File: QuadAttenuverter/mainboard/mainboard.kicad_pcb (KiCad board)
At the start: 2 copper layers, 35.6 x 108 mm, 65 parts, among them U1 LM324, U2 LM324, U3 LM324, U4 LM324, U5 LM324

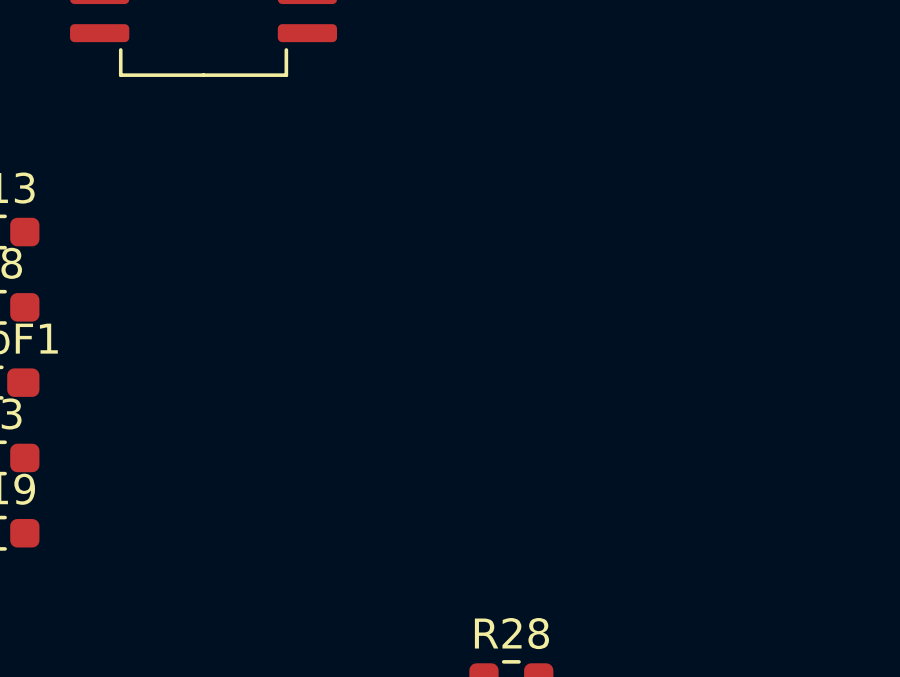
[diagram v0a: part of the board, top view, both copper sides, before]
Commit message: Add resistors to make pots more center sensitive
Idea from here:
https://kassu2000.blogspot.com/2018/04/precision-attenuverter-mixer.html
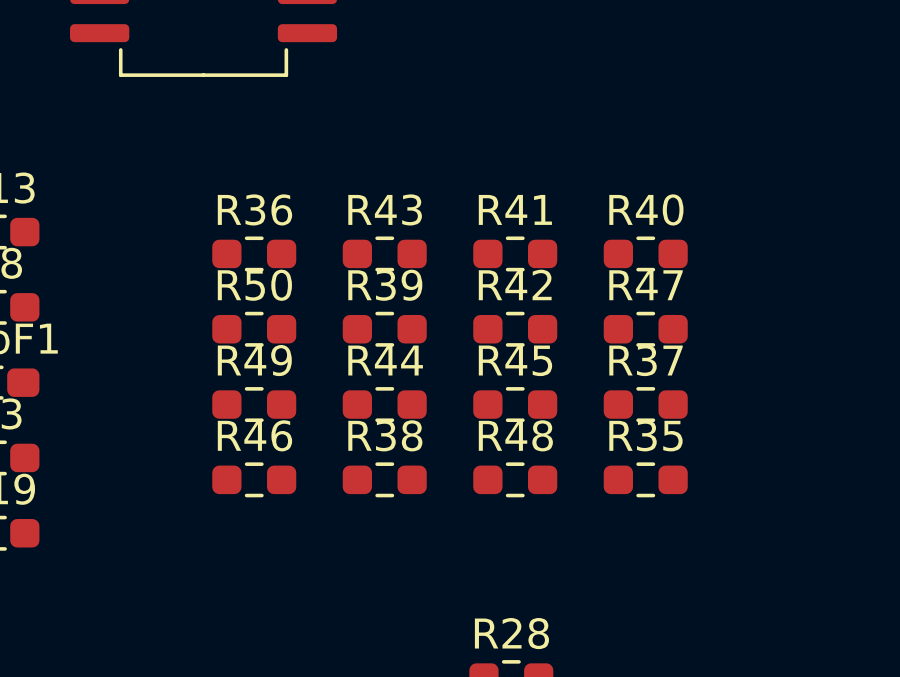
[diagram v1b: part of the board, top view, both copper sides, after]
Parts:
- added R35: 47k, Resistor_SMD:R_0603_1608Metric_Pad0.98x0.95mm_HandSolder, F.Cu at (208.8, 121.5)
- added R36: 47k, Resistor_SMD:R_0603_1608Metric_Pad0.98x0.95mm_HandSolder, F.Cu at (195.8, 114.0)
- added R37: 47k, Resistor_SMD:R_0603_1608Metric_Pad0.98x0.95mm_HandSolder, F.Cu at (208.8, 119.0)
- added R38: 47k, Resistor_SMD:R_0603_1608Metric_Pad0.98x0.95mm_HandSolder, F.Cu at (200.1, 121.5)
- added R39: 47k, Resistor_SMD:R_0603_1608Metric_Pad0.98x0.95mm_HandSolder, F.Cu at (200.1, 116.5)
- added R40: 47k, Resistor_SMD:R_0603_1608Metric_Pad0.98x0.95mm_HandSolder, F.Cu at (208.8, 114.0)
- added R41: 47k, Resistor_SMD:R_0603_1608Metric_Pad0.98x0.95mm_HandSolder, F.Cu at (204.4, 114.0)
- added R42: 47k, Resistor_SMD:R_0603_1608Metric_Pad0.98x0.95mm_HandSolder, F.Cu at (204.4, 116.5)
- added R43: 47k, Resistor_SMD:R_0603_1608Metric_Pad0.98x0.95mm_HandSolder, F.Cu at (200.1, 114.0)
- added R44: 47k, Resistor_SMD:R_0603_1608Metric_Pad0.98x0.95mm_HandSolder, F.Cu at (200.1, 119.0)
- added R45: 47k, Resistor_SMD:R_0603_1608Metric_Pad0.98x0.95mm_HandSolder, F.Cu at (204.4, 119.0)
- added R46: 47k, Resistor_SMD:R_0603_1608Metric_Pad0.98x0.95mm_HandSolder, F.Cu at (195.8, 121.5)
- added R47: 47k, Resistor_SMD:R_0603_1608Metric_Pad0.98x0.95mm_HandSolder, F.Cu at (208.8, 116.5)
- added R48: 47k, Resistor_SMD:R_0603_1608Metric_Pad0.98x0.95mm_HandSolder, F.Cu at (204.4, 121.5)
- added R49: 47k, Resistor_SMD:R_0603_1608Metric_Pad0.98x0.95mm_HandSolder, F.Cu at (195.8, 119.0)
- added R50: 47k, Resistor_SMD:R_0603_1608Metric_Pad0.98x0.95mm_HandSolder, F.Cu at (195.8, 116.5)

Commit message: Final preparations for board splitup
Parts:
- added J1: Conn_01x09, Connector_PinHeader_2.54mm:PinHeader_1x09_P2.54mm_Vertical, F.Cu at (101.0, 115.8)
- added J2: Conn_02x10_Counter_Clockwise, Connector_PinHeader_2.54mm:PinHeader_2x10_P2.54mm_Vertical, F.Cu at (89.7, 45.6)
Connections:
- net Net-(IN1-PadT) renamed /IN1
- net Net-(IN2-PadT) renamed /IN3
- net Net-(IN3-PadT) renamed /IN2
- net Net-(IN4-PadT) renamed /IN4
- net Net-(OUT1-PadT) renamed /OUT1
- net Net-(OUT2-PadT) renamed /OUT3
- net Net-(OUT3-PadT) renamed /OUT2
- net Net-(OUT4-PadT) renamed /OUT4
- net Net-(R13-Pad1) renamed /GAIN3IN
- net Net-(R14-Pad1) renamed /GAIN2IN
- net Net-(R15-Pad1) renamed /GAIN4IN
- net Net-(R2-Pad1) renamed /GAIN1IN
- net Net-(R35-Pad2) renamed /GAIN3OUT
- net Net-(R36-Pad2) renamed /GAIN1OUT
- net Net-(R37-Pad2) renamed /GAIN2OUT
- net Net-(R38-Pad2) renamed /GAIN4OUT
- net Net-(R43-Pad2) renamed /OFFSET3
- net Net-(R45-Pad2) renamed /OFFSET1
- net Net-(R47-Pad2) renamed /OFFSET2
- net Net-(R49-Pad2) renamed /OFFSET4
- D1 pad 1: Net-(D1-Pad1) -> GND
- D1 pad 2: Net-(D1-Pad2) -> /LED1
- D2 pad 1: Net-(D2-Pad1) -> GND
- D2 pad 2: Net-(D2-Pad2) -> /LED2
- D3 pad 1: Net-(D3-Pad1) -> GND
- D3 pad 2: Net-(D3-Pad2) -> /LED3
- D4 pad 1: Net-(D4-Pad1) -> GND
- D4 pad 2: Net-(D4-Pad2) -> /LED4
- R31 pad 1: Net-(D1-Pad1) -> Net-(R31-Pad1)
- R31 pad 2: GND -> /LED1
- R32 pad 1: Net-(D2-Pad1) -> Net-(R32-Pad1)
- R32 pad 2: GND -> /LED2
- R33 pad 1: Net-(D3-Pad1) -> Net-(R33-Pad1)
- R33 pad 2: GND -> /LED3
- R34 pad 1: Net-(D4-Pad1) -> Net-(R34-Pad1)
- R34 pad 2: GND -> /LED4
- U5 pad 1: Net-(D1-Pad2) -> Net-(R31-Pad1)
- U5 pad 14: Net-(D4-Pad2) -> Net-(R34-Pad1)
- U5 pad 7: Net-(D2-Pad2) -> Net-(R32-Pad1)
- U5 pad 8: Net-(D3-Pad2) -> Net-(R33-Pad1)

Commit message: Fixed duplicate net names for LEDn
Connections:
- 22pF1 pad 2: /LED1 -> /LEDSIG1
- 22pF2 pad 2: /LED3 -> /LEDSIG3
- 22pF3 pad 2: /LED2 -> /LEDSIG2
- 22pF4 pad 2: /LED4 -> /LEDSIG4
- R28 pad 1: /LED3 -> /LEDSIG3
- R29 pad 1: /LED2 -> /LEDSIG2
- R30 pad 1: /LED4 -> /LEDSIG4
- R7 pad 1: /LED1 -> /LEDSIG1
- U1 pad 8: /LED1 -> /LEDSIG1
- U2 pad 8: /LED3 -> /LEDSIG3
- U3 pad 8: /LED2 -> /LEDSIG2
- U4 pad 8: /LED4 -> /LEDSIG4
- U5 pad 10: /LED3 -> /LEDSIG3
- U5 pad 12: /LED4 -> /LEDSIG4
- U5 pad 3: /LED1 -> /LEDSIG1
- U5 pad 5: /LED2 -> /LEDSIG2
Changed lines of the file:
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@@
   (net 57 "Net-(R33-Pad1)")
   (net 58 "Net-(R34-Pad1)")
+  (net 59 "/LEDSIG1")
+  (net 60 "/LEDSIG3")
+  (net 61 "/LEDSIG2")
+  (net 62 "/LEDSIG4")
   (footprint "Potentiometer_THT:Potentiometer_Alps_RK09K_Single_Vertical" (layer "F.Cu")
     (at 116.8 57.71 180)
@@
       (net 24 "Net-(R3-Pad2)") (pintype "output"))
     (pad "8" smd roundrect (at 3.4625 3.81) (size 1.975 0.6) (layers "F.Cu" "F.Paste" "F.Mask") (roundrect_rratio 0.25)
-      (net 2 "/LED1") (pintype "output"))
+      (net 59 "/LEDSIG1") (pintype "output"))
     (pad "9" smd roundrect (at 3.4625 2.54) (size 1.975 0.6) (layers "F.Cu" "F.Paste" "F.Mask") (roundrect_rratio 0.25)
       (net 1 "Net-(22pF1-Pad1)") (pinfunction "-") (pintype "input"))
@@
       (net 37 "Net-(R16-Pad2)") (pintype "output"))
     (pad "8" smd roundrect (at 3.4625 3.81) (size 1.975 0.6) (layers "F.Cu" "F.Paste" "F.Mask") (roundrect_rratio 0.25)
-      (net 51 "/LED3") (pintype "output"))
+      (net 60 "/LEDSIG3") (pintype "output"))
     (pad "9" smd roundrect (at 3.4625 2.54) (size 1.975 0.6) (layers "F.Cu" "F.Paste" "F.Mask") (roundrect_rratio 0.25)
       (net 3 "Net-(22pF2-Pad1)") (pinfunction "-") (pintype "input"))
@@
       (net 3 "Net-(22pF2-Pad1)") (pintype "passive"))
     (pad "2" smd roundrect (at 0.8625 0) (size 1.075 0.95) (layers "F.Cu" "F.Paste" "F.Mask") (roundrect_rratio 0.25)
-      (net 51 "/LED3") (pintype "passive"))
+      (net 60 "/LEDSIG3") (pintype "passive"))
     (model "${KICAD6_3DMODEL_DIR}/Capacitor_SMD.3dshapes/C_0603_1608Metric.wrl"
       (offset (xyz 0 0 0))
@@
       (net 4 "Net-(22pF3-Pad1)") (pintype "passive"))
     (pad "2" smd roundrect (at 0.8625 0) (size 1.075 0.95) (layers "F.Cu" "F.Paste" "F.Mask") (roundrect_rratio 0.25)
-      (net 52 "/LED2") (pintype "passive"))
+      (net 61 "/LEDSIG2") (pintype "passive"))
     (model "${KICAD6_3DMODEL_DIR}/Capacitor_SMD.3dshapes/C_0603_1608Metric.wrl"
       (offset (xyz 0 0 0))
@@
       (net 7 "GND") (pinfunction "-") (pintype "input"))
     (pad "3" smd roundrect (at -3.4625 -1.27) (size 1.975 0.6) (layers "F.Cu" "F.Paste" "F.Mask") (roundrect_rratio 0.25)
-      (net 2 "/LED1") (pinfunction "+") (pintype "input"))
+      (net 59 "/LEDSIG1") (pinfunction "+") (pintype "input"))
     (pad "4" smd roundrect (at -3.4625 0) (size 1.975 0.6) (layers "F.Cu" "F.Paste" "F.Mask") (roundrect_rratio 0.25)
       (net 26 "+12V") (pinfunction "V+") (pintype "power_in"))
     (pad "5" smd roundrect (at -3.4625 1.27) (size 1.975 0.6) (layers "F.Cu" "F.Paste" "F.Mask") (roundrect_rratio 0.25)
-      (net 52 "/LED2") (pinfunction "+") (pintype "input"))
+      (net 61 "/LEDSIG2") (pinfunction "+") (pintype "input"))
     (pad "6" smd roundrect (at -3.4625 2.54) (size 1.975 0.6) (layers "F.Cu" "F.Paste" "F.Mask") (roundrect_rratio 0.25)
       (net 7 "GND") (pinfunction "-") (pintype "input"))
@@
       (net 7 "GND") (pinfunction "-") (pintype "input"))
     (pad "10" smd roundrect (at 3.4625 1.27) (size 1.975 0.6) (layers "F.Cu" "F.Paste" "F.Mask") (roundrect_rratio 0.25)
-      (net 51 "/LED3") (pinfunction "+") (pintype "input"))
+      (net 60 "/LEDSIG3") (pinfunction "+") (pintype "input"))
     (pad "11" smd roundrect (at 3.4625 0) (size 1.975 0.6) (layers "F.Cu" "F.Paste" "F.Mask") (roundrect_rratio 0.25)
       (net 27 "-12V") (pinfunction "V-") (pintype "power_in"))
     (pad "12" smd roundrect (at 3.4625 -1.27) (size 1.975 0.6) (layers "F.Cu" "F.Paste" "F.Mask") (roundrect_rratio 0.25)
-      (net 53 "/LED4") (pinfunction "+") (pintype "input"))
+      (net 62 "/LEDSIG4") (pinfunction "+") (pintype "input"))
     (pad "13" smd roundrect (at 3.4625 -2.54) (size 1.975 0.6) (layers "F.Cu" "F.Paste" "F.Mask") (roundrect_rratio 0.25)
       (net 7 "GND") (pinfunction "-") (pintype "input"))
@@
     (fp_line (start 0.8 0.4125) (end -0.8 0.4125) (layer "F.Fab") (width 0.1))
     (pad "1" smd roundrect (at -0.9125 0) (size 0.975 0.95) (layers "F.Cu" "F.Paste" "F.Mask") (roundrect_rratio 0.25)
-      (net 51 "/LED3") (pintype "passive"))
+      (net 60 "/LEDSIG3") (pintype "passive"))
     (pad "2" smd roundrect (at 0.9125 0) (size 0.975 0.95) (layers "F.Cu" "F.Paste" "F.Mask") (roundrect_rratio 0.25)
       (net 17 "/OUT3") (pintype "passive"))
@@
       (net 5 "Net-(22pF4-Pad1)") (pintype "passive"))
     (pad "2" smd roundrect (at 0.8625 0) (size 1.075 0.95) (layers "F.Cu" "F.Paste" "F.Mask") (roundrect_rratio 0.25)
-      (net 53 "/LED4") (pintype "passive"))
+      (net 62 "/LEDSIG4") (pintype "passive"))
     (model "${KICAD6_3DMODEL_DIR}/Capacitor_SMD.3dshapes/C_0603_1608Metric.wrl"
       (offset (xyz 0 0 0))
@@
       (net 39 "Net-(R18-Pad2)") (pintype "output"))
     (pad "8" smd roundrect (at 3.4625 3.81) (size 1.975 0.6) (layers "F.Cu" "F.Paste" "F.Mask") (roundrect_rratio 0.25)
-      (net 53 "/LED4") (pintype "output"))
+      (net 62 "/LEDSIG4") (pintype "output"))
     (pad "9" smd roundrect (at 3.4625 2.54) (size 1.975 0.6) (layers "F.Cu" "F.Paste" "F.Mask") (roundrect_rratio 0.25)
       (net 5 "Net-(22pF4-Pad1)") (pinfunction "-") (pintype "input"))
@@
     (fp_line (start -0.8 0.4125) (end -0.8 -0.4125) (layer "F.Fab") (width 0.1))
     (pad "1" smd roundrect (at -0.9125 0) (size 0.975 0.95) (layers "F.Cu" "F.Paste" "F.Mask") (roundrect_rratio 0.25)
-      (net 52 "/LED2") (pintype "passive"))
+      (net 61 "/LEDSIG2") (pintype "passive"))
     (pad "2" smd roundrect (at 0.9125 0) (size 0.975 0.95) (layers "F.Cu" "F.Paste" "F.Mask") (roundrect_rratio 0.25)
       (net 15 "/OUT2") (pintype "passive"))
@@
       (net 38 "Net-(R17-Pad2)") (pintype "output"))
     (pad "8" smd roundrect (at 3.4625 3.81) (size 1.975 0.6) (layers "F.Cu" "F.Paste" "F.Mask") (roundrect_rratio 0.25)
-      (net 52 "/LED2") (pintype "output"))
+      (net 61 "/LEDSIG2") (pintype "output"))
     (pad "9" smd roundrect (at 3.4625 2.54) (size 1.975 0.6) (layers "F.Cu" "F.Paste" "F.Mask") (roundrect_rratio 0.25)
       (net 4 "Net-(22pF3-Pad1)") (pinfunction "-") (pintype "input"))
@@
     (fp_line (start -0.8 0.4125) (end -0.8 -0.4125) (layer "F.Fab") (width 0.1))
     (pad "1" smd roundrect (at -0.9125 0) (size 0.975 0.95) (layers "F.Cu" "F.Paste" "F.Mask") (roundrect_rratio 0.25)
-      (net 2 "/LED1") (pintype "passive"))
+      (net 59 "/LEDSIG1") (pintype "passive"))
     (pad "2" smd roundrect (at 0.9125 0) (size 0.975 0.95) (layers "F.Cu" "F.Paste" "F.Mask") (roundrect_rratio 0.25)
       (net 13 "/OUT1") (pintype "passive"))
@@
       (net 1 "Net-(22pF1-Pad1)") (pintype "passive"))
     (pad "2" smd roundrect (at 0.8625 0) (size 1.075 0.95) (layers "F.Cu" "F.Paste" "F.Mask") (roundrect_rratio 0.25)
-      (net 2 "/LED1") (pintype "passive"))
+      (net 59 "/LEDSIG1") (pintype "passive"))
     (model "${KICAD6_3DMODEL_DIR}/Capacitor_SMD.3dshapes/C_0603_1608Metric.wrl"
       (offset (xyz 0 0 0))
@@
     (fp_line (start 0.8 0.4125) (end -0.8 0.4125) (layer "F.Fab") (width 0.1))
     (pad "1" smd roundrect (at -0.9125 0) (size 0.975 0.95) (layers "F.Cu" "F.Paste" "F.Mask") (roundrect_rratio 0.25)
-      (net 53 "/LED4") (pintype "passive"))
+      (net 62 "/LEDSIG4") (pintype "passive"))
     (pad "2" smd roundrect (at 0.9125 0) (size 0.975 0.95) (layers "F.Cu" "F.Paste" "F.Mask") (roundrect_rratio 0.25)
       (net 19 "/OUT4") (pintype "passive"))

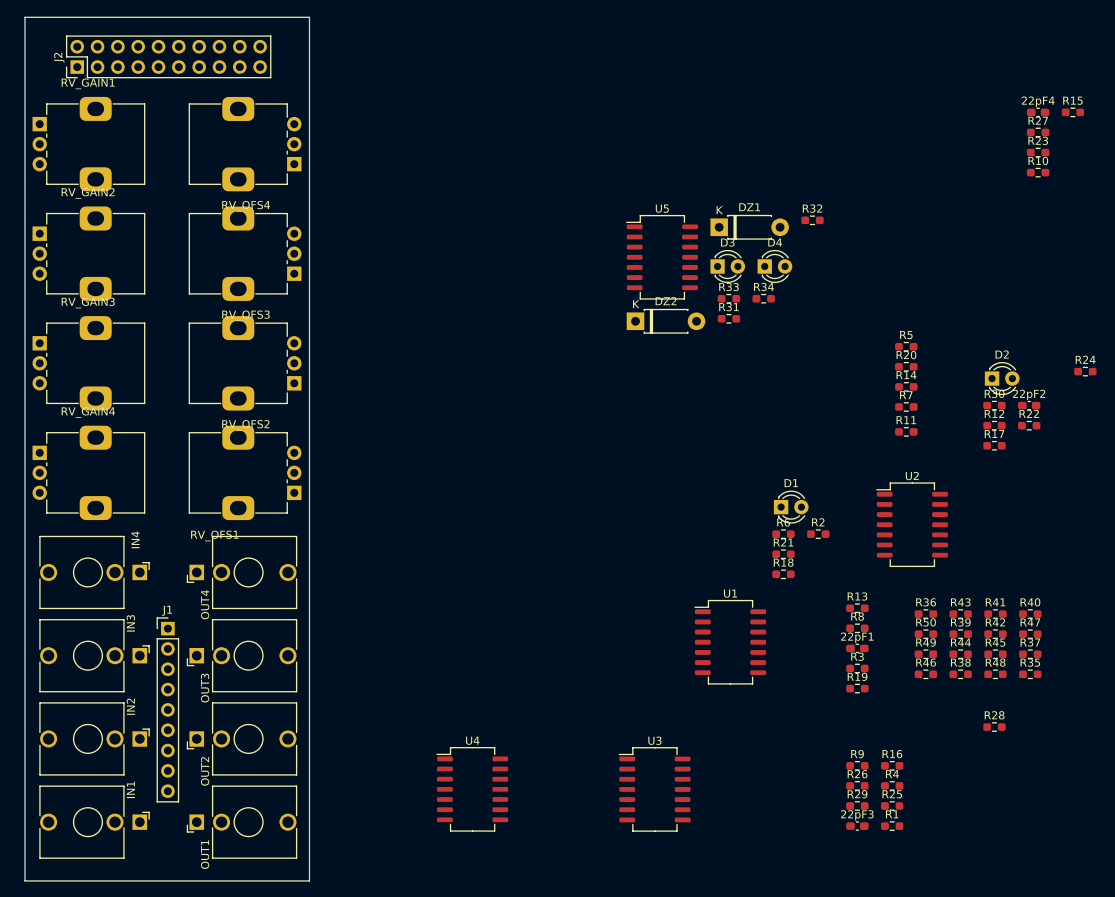
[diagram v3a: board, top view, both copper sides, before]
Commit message: Initial routing of ioboard
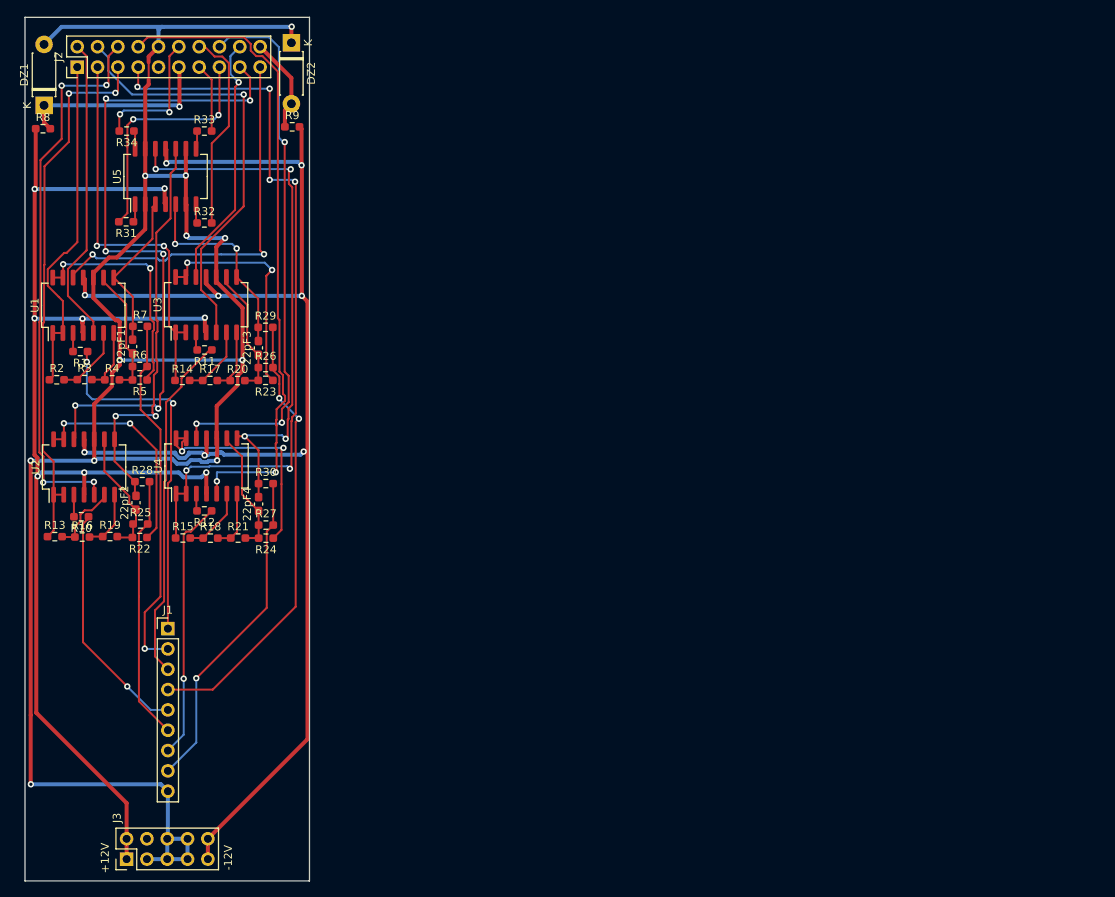
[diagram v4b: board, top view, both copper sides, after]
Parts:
- removed D1, D2, D3, D4: LED_Dual_Bidirectional, LED_THT:LED_D3.0mm
- removed IN1, IN2, IN3, IN4, OUT1, OUT2, OUT3, OUT4: AudioJack2_SwitchT, Connector_Audio:Jack_3.5mm_QingPu_WQP-PJ398SM_Vertical_CircularHoles
- removed R35, R36, R37, R38, R39, R40, R41, R42, R43, R44, R45, R46, R47, R48, R49, R50: 47k, Resistor_SMD:R_0603_1608Metric_Pad0.98x0.95mm_HandSolder
- removed RV_GAIN1, RV_GAIN2, RV_GAIN3, RV_GAIN4, RV_OFS1, RV_OFS2, RV_OFS3, RV_OFS4: 100k, Potentiometer_THT:Potentiometer_Alps_RK09K_Single_Vertical
- added J3: Conn_02x05_Odd_Even, Connector_PinHeader_2.54mm:PinHeader_2x05_P2.54mm_Vertical, F.Cu at (95.8, 144.6)
- moved R10 127.1 mm to (90.2, 101.8), turned to 180 degrees
- moved R15 123.3 mm to (102.9, 104.4)
- moved R8 119.4 mm to (85.4, 53.3)
- moved R1 117.6 mm to (90.0, 81.1), turned to 180 degrees
- moved 22pF2 112.3 mm to (97.0, 100.0), turned to 90 degrees
- moved R22 112.1 mm to (97.5, 104.4), turned to 180 degrees
- moved R28 110.9 mm to (97.8, 97.4)
- moved R4 109.9 mm to (94.0, 84.7)
- moved 22pF4 109.0 mm to (112.3, 100.2), turned to 90 degrees
- moved R27 108.3 mm to (113.3, 102.8)
- moved R9 106.6 mm to (116.5, 53.0)
- moved R16 105.2 mm to (90.3, 104.3)
- moved R24 104.5 mm to (113.3, 104.5), turned to 180 degrees
- moved U2 103.8 mm to (90.5, 95.6), turned to 90 degrees
- moved R3 103.1 mm to (90.6, 84.6)
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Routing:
- net GND: track 0.00 -> 263.2 mm, vias 0 -> 11
- net -12V: track 0.00 -> 181.1 mm, vias 0 -> 8
- net +12V: track 0.00 -> 167.4 mm, vias 0 -> 8
- net /GAIN4IN: track 0.00 -> 93.1 mm, vias 0 -> 6
- net /OFFSET3: track 0.00 -> 83.7 mm, vias 0 -> 6
- net /GAIN4OUT: track 0.00 -> 81.3 mm, vias 0 -> 2
- net /GAIN3OUT: track 0.00 -> 70.0 mm, vias 0 -> 4
- net /OFFSET4: track 0.00 -> 68.9 mm, vias 0 -> 3
- net /LEDSIG4: track 0.00 -> 68.5 mm, vias 0 -> 4
- net /GAIN3IN: track 0.00 -> 68.1 mm, vias 0 -> 2
- net /OUT2: track 0.00 -> 56.7 mm, vias 0 -> 2
- net /GAIN2OUT: track 0.00 -> 54.4 mm, vias 0 -> 1
- net /LEDSIG3: track 0.00 -> 51.3 mm, vias 0 -> 2
- net /OFFSET1: track 0.00 -> 49.7 mm, vias 0 -> 2
- net /GAIN2IN: track 0.00 -> 49.6 mm, vias 0 -> 2
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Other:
- board text added: "+12V"
- board text added: "-12V"
